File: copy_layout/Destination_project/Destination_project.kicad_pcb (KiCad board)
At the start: 2 copper layers, 11 parts, among them Q1 CSD19531KCS, Q2 CSD19531KCS, U1 LAUNCHXL-F28379D, U2 IR2181, U3 LTS_15

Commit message: Delna verzija
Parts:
- added C4: 100n, Passives:C1206M, F.Cu at (127.1, 116.9)
- added C5: C1206, Passives:C1206M, F.Cu at (165.0, 109.7)
- added C6: 100n, Passives:C1206M, F.Cu at (136.6, 125.6)
- added C7: 100n, Passives:C1206M, F.Cu at (128.1, 132.1)
- added D2: LL4148, Discretes:D_MiniMELF, F.Cu at (121.1, 117.0)
- added D3: LL4148, Discretes:D_MiniMELF, F.Cu at (117.0, 137.6)
- added J1: Pusa_4mm, Connector:Pusa_4mm, F.Cu at (91.2, 111.0)
- added J2: Pusa_4mm, Connector:Pusa_4mm, F.Cu at (106.3, 111.0)
- added Q3: CSD19531KCS, Discretes:TO-220, F.Cu at (121.2, 106.7)
- added Q4: CSD19531KCS, Discretes:TO-220, F.Cu at (121.2, 112.7)
- added Q5: CSD19531KCS, Discretes:TO-220, F.Cu at (117.0, 127.3)
- added Q6: CSD19531KCS, Discretes:TO-220, F.Cu at (117.0, 133.3)
- added R3: 22R, Passives:R1206M, F.Cu at (140.8, 105.0)
- added R4: 22R, Passives:R1206M, F.Cu at (132.3, 111.5)
- added R5: R_Shunt, Passives:RM, F.Cu at (155.2, 109.0)
- added R6: 22R, Passives:R1206M, F.Cu at (122.9, 137.6)
- added R7: 22R, Passives:R1206M, F.Cu at (133.7, 132.1)
- added U4: INA240, Package_SO:TSSOP-8_4.4x3mm_P0.65mm, F.Cu at (166.7, 105.8)
- added U5: IR2181, Package_SO:SO8, F.Cu at (129.6, 127.3)
- U3: value LTS_15 -> IR2181; footprint Sensor_Current:LTS_15 -> Package_SO:SO8
- moved U3 88.5 mm to (133.8, 106.7)
- moved C3 83.0 mm to (137.8, 111.5)
- moved C1 55.6 mm to (103.5, 132.1)
- moved C2 44.6 mm to (98.0, 132.1)
- moved D1 44.5 mm to (86.8, 137.6)
- moved R2 33.1 mm to (106.5, 125.6)
- moved U2 33.1 mm to (99.4, 127.3)
- moved R1 28.0 mm to (92.8, 137.6)
- moved Q1 20.8 mm to (86.9, 127.3)
- moved Q2 20.8 mm to (86.9, 133.3)
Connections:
- C1 pad 1: +12V -> +15V
- C1 pad 2: GND -> -VDC
- C2 pad 2: Net-(C2-Pad2) -> /power/OUT
- C3 pad 1: GND -> +15V
- C3 pad 2: +3V3 -> -VDC
- D1 pad 1: Net-(C2-Pad2) -> Net-(C2-Pad1)
- D1 pad 2: +12V -> +15V
- Q1 pad 2: +12V -> +VDC
- Q1 pad 3: Net-(C2-Pad1) -> /power/OUT
- Q2 pad 2: Net-(C2-Pad1) -> /power/OUT
- Q2 pad 3: GND -> -VDC
- U1 pad 20: GND -> -VDC
- U1 pad 22: GND -> -VDC
- U1 pad 24: /Leg1/TOK -> /Leg/Current
- U1 pad 37: Net-(U1-Pad37) -> /power/Ql
- U1 pad 38: Net-(U1-Pad38) -> /power/QH
- U1 pad 39: /Leg1/LIN -> /Leg/QL
- U1 pad 40: /Leg1/HIN -> /Leg/QH
- U1 pad 60: GND -> -VDC
- U1 pad 62: GND -> -VDC
- U2 pad 1: /Leg1/HIN -> /power/QH
- U2 pad 2: /Leg1/LIN -> /power/Ql
- U2 pad 3: GND -> -VDC
- U2 pad 5: +12V -> +15V
- U2 pad 6: Net-(C2-Pad1) -> /power/OUT
- U2 pad 8: Net-(C2-Pad2) -> Net-(C2-Pad1)
- U3 pad 1: Net-(C2-Pad1) -> /Leg/QH
- U3 pad 2: Net-(C2-Pad1) -> /Leg/QL
- U3 pad 3: Net-(C2-Pad1) -> -VDC
- U3 pad 4: Net-(U3-Pad4) -> Net-(R4-Pad1)
- U3 pad 5: Net-(U3-Pad4) -> +15V
- U3 pad 6: Net-(U3-Pad4) -> /Leg/Sensor/IN

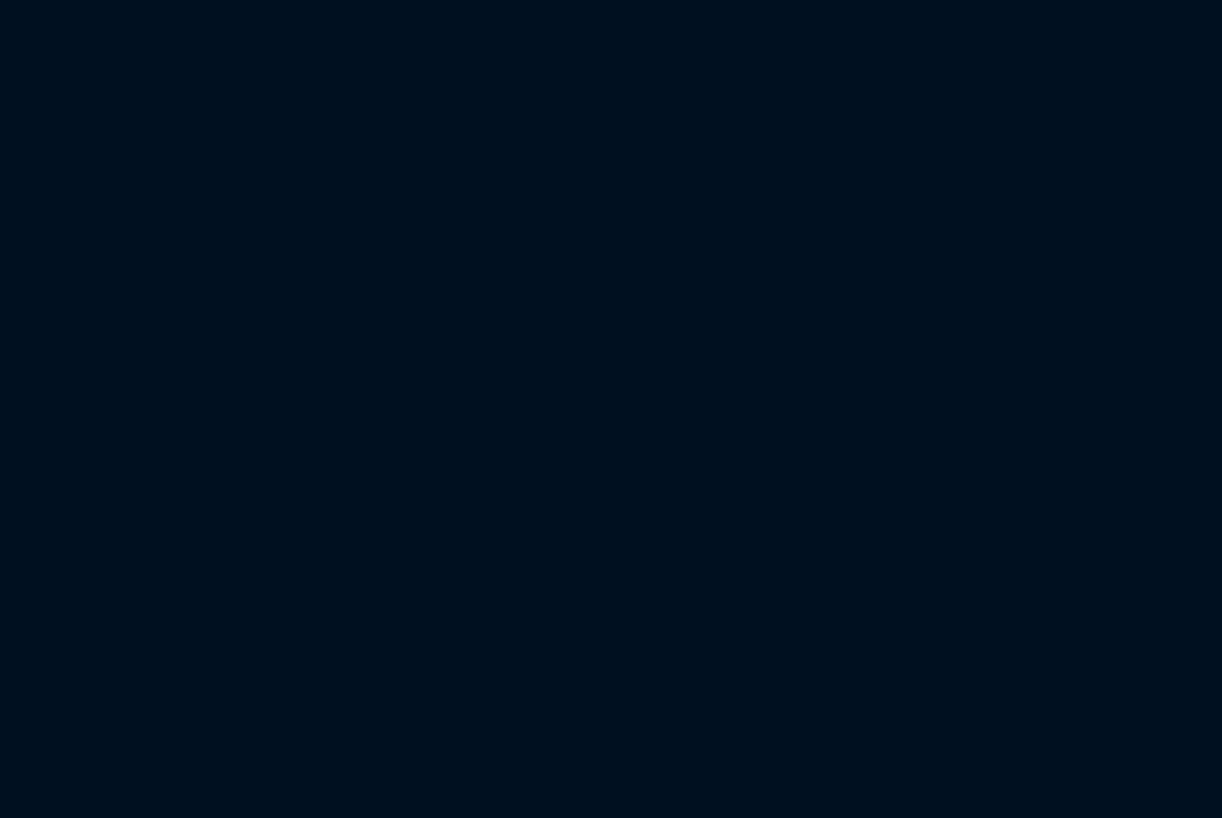
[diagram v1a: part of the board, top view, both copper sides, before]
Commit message: Modified test project. Successfule began importing layout
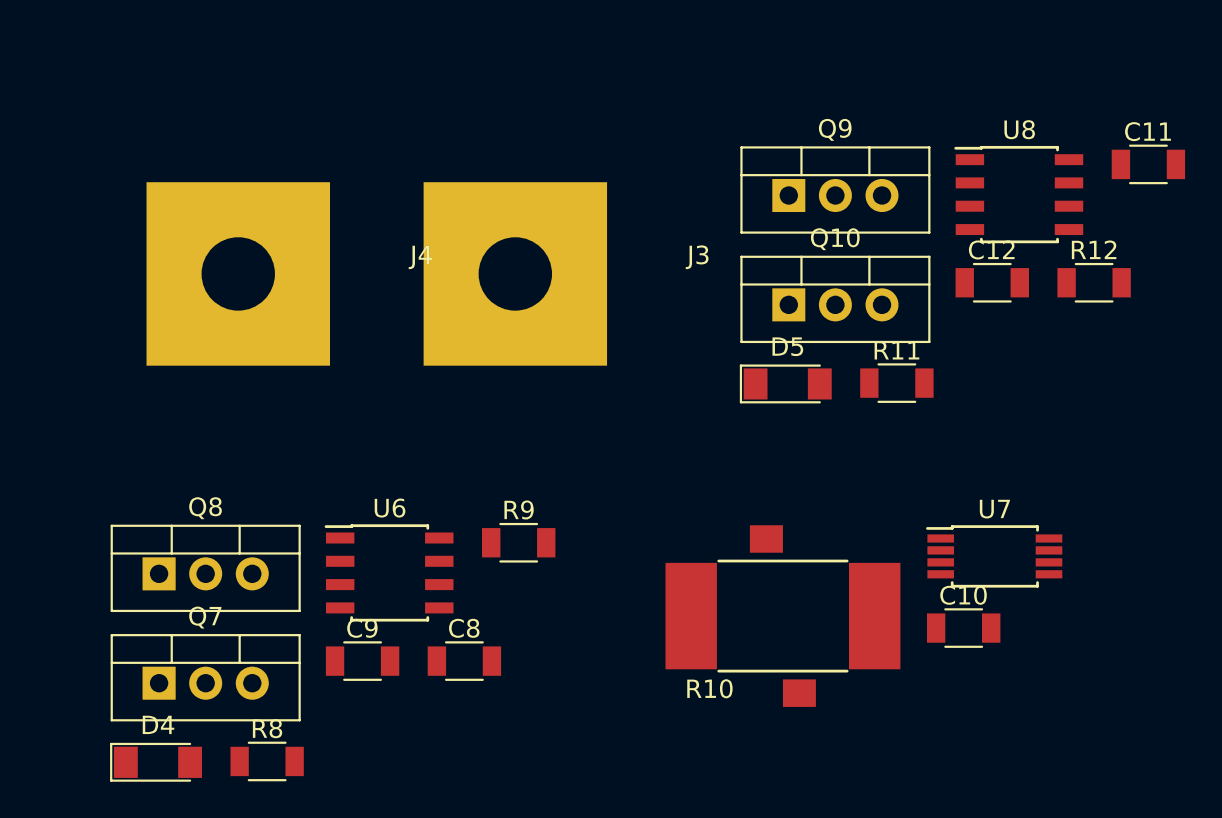
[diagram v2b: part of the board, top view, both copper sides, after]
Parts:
- added C10: C1206, Passives:C1206M, F.Cu at (210.1, 147.4)
- added C11: 100n, Passives:C1206M, F.Cu at (220.2, 122.2)
- added C12: 100n, Passives:C1206M, F.Cu at (211.7, 128.6)
- added C8: 100n, Passives:C1206M, F.Cu at (182.9, 149.2)
- added C9: 100n, Passives:C1206M, F.Cu at (177.3, 149.2)
- added D4: LL4148, Discretes:D_MiniMELF, F.Cu at (166.2, 154.7)
- added D5: LL4148, Discretes:D_MiniMELF, F.Cu at (200.5, 134.1)
- added J3: Pusa_4mm, Connector:Pusa_4mm, F.Cu at (185.7, 128.1)
- added J4: Pusa_4mm, Connector:Pusa_4mm, F.Cu at (170.6, 128.1)
- added Q10: CSD19531KCS, Discretes:TO-220, F.Cu at (200.6, 129.8)
- added Q7: CSD19531KCS, Discretes:TO-220, F.Cu at (166.2, 150.4)
- added Q8: CSD19531KCS, Discretes:TO-220, F.Cu at (166.2, 144.5)
- added Q9: CSD19531KCS, Discretes:TO-220, F.Cu at (200.6, 123.8)
- added R10: R_Shunt, Passives:RM, F.Cu at (200.2, 146.8)
- added R11: 22R, Passives:R1206M, F.Cu at (206.4, 134.1)
- added R12: 22R, Passives:R1206M, F.Cu at (217.2, 128.6)
- added R8: 22R, Passives:R1206M, F.Cu at (172.1, 154.7)
- added R9: 22R, Passives:R1206M, F.Cu at (185.8, 142.8)
- added U6: IR2181, Package_SO:SO8, F.Cu at (178.8, 144.4)
- added U7: INA240, Package_SO:TSSOP-8_4.4x3mm_P0.65mm, F.Cu at (211.8, 143.5)
- added U8: IR2181, Package_SO:SO8, F.Cu at (213.1, 123.8)
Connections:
- U1 pad 63: Net-(U1-Pad63) -> /Leg 2/Current
- U1 pad 79: Net-(U1-Pad79) -> /Leg 2/QL
- U1 pad 80: Net-(U1-Pad80) -> /Leg 2/QH

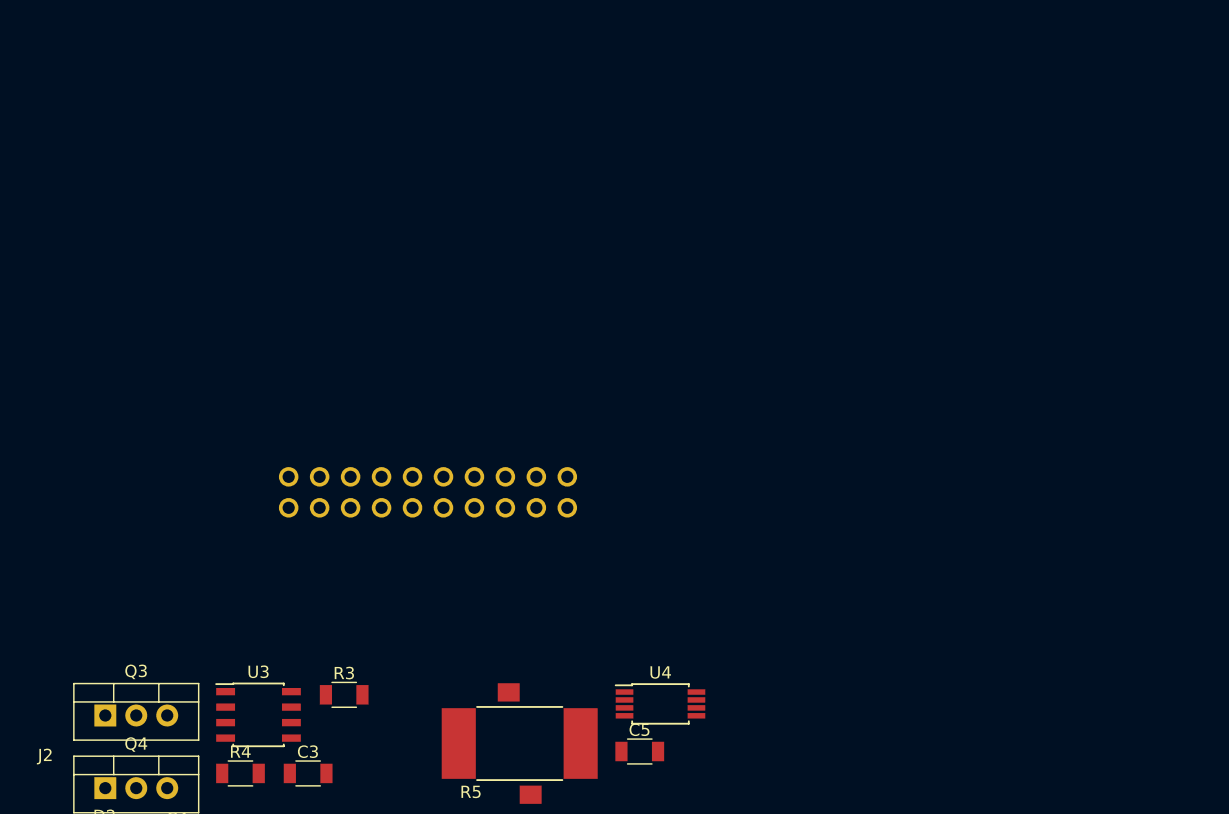
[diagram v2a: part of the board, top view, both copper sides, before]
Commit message: Updated destination project
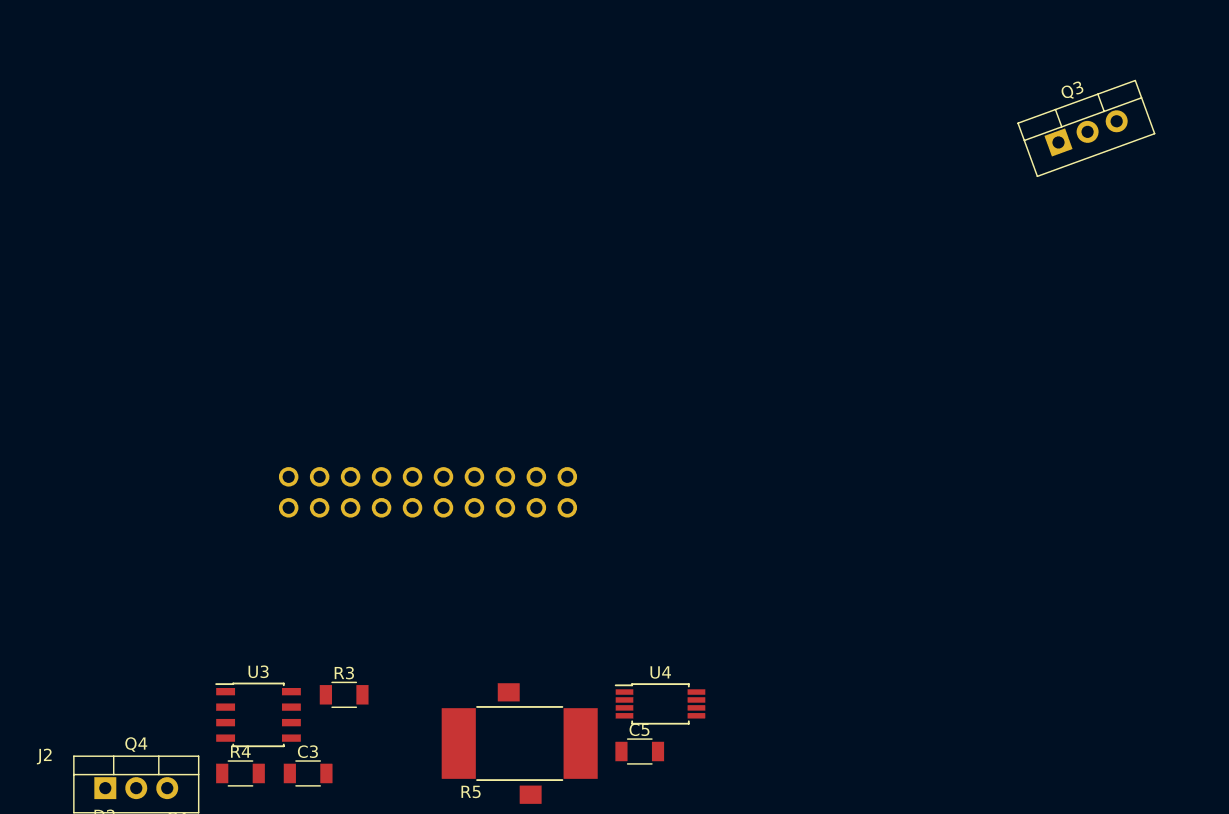
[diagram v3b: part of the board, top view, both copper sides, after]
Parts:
- moved Q3 91.2 mm to (199.4, 59.7), turned to 20 degrees
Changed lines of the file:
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@@
   )
   (module Discretes:TO-220 (layer F.Cu)
-    (at 121.185 106.705)
+    (at 199.39 59.69 20)
     (descr "TO-220-3, Vertical, RM 2.54mm")
     (tags "TO-220-3 Vertical RM 2.54mm")
-    (fp_text reference Q3 (at 2.54 -3.62) (layer F.SilkS)
+    (fp_text reference Q3 (at 2.54 -3.62 20) (layer F.SilkS)
       (effects (font (size 1 1) (thickness 0.15)))
     )
-    (fp_text value CSD19531KCS (at 2.54 3.92) (layer F.Fab) hide
+    (fp_text value CSD19531KCS (at 2.54 3.92 20) (layer F.Fab) hide
       (effects (font (size 1 1) (thickness 0.15)))
     )
@@
     (fp_line (start -2.46 1.9) (end 7.54 1.9) (layer F.Fab) (width 0.1))
     (fp_line (start -2.46 -2.5) (end -2.46 1.9) (layer F.Fab) (width 0.1))
-    (fp_text user %R (at 2.54 -3.62) (layer F.Fab)
+    (fp_text user %R (at 2.54 -3.62 20) (layer F.Fab)
       (effects (font (size 1 1) (thickness 0.15)))
     )
-    (pad 3 thru_hole oval (at 5.08 0) (size 1.8 1.8) (drill 1) (layers *.Cu *.Mask)
+    (pad 3 thru_hole oval (at 5.08 0 20) (size 1.8 1.8) (drill 1) (layers *.Cu *.Mask)
       (net 75 /Leg/Sensor/IN))
-    (pad 2 thru_hole oval (at 2.54 0) (size 1.8 1.8) (drill 1) (layers *.Cu *.Mask)
+    (pad 2 thru_hole oval (at 2.54 0 20) (size 1.8 1.8) (drill 1) (layers *.Cu *.Mask)
       (net 80 +VDC))
-    (pad 1 thru_hole rect (at 0 0) (size 1.8 1.8) (drill 1) (layers *.Cu *.Mask)
+    (pad 1 thru_hole rect (at 0 0 20) (size 1.8 1.8) (drill 1) (layers *.Cu *.Mask)
       (net 81 "Net-(Q3-Pad1)"))
     (model ${KISYS3DMOD}/Package_TO_SOT_THT.3dshapes/TO-220-3_Vertical.wrl

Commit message: changed test project Added gif animation
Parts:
- moved J3 103.4 mm to (192.2, 24.9)
- moved J4 103.4 mm to (177.1, 24.9)
- moved C4 101.2 mm to (192.3, 39.6)
- moved Q4 88.1 mm to (172.7, 41.3)
- moved R4 86.9 mm to (189.4, 46.0)
- moved D2 83.3 mm to (172.7, 51.5)
- moved U3 83.3 mm to (185.3, 41.2)
- moved C3 80.0 mm to (183.8, 46.0)
- moved R11 77.5 mm to (192.3, 57.8)
- moved J2 77.5 mm to (28.8, 109.6)
- moved Q10 75.6 mm to (172.7, 59.5)
- moved R12 72.4 mm to (183.8, 64.3)
- moved C10 70.7 mm to (186.4, 80.8)
- moved R10 70.7 mm to (176.6, 80.1)
- moved U7 70.7 mm to (188.1, 76.9)
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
